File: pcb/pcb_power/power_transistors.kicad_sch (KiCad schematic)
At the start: 6 parts, among them Q1 BD139, Q2 BD139, Q3 BD249C, Q4 BD249C

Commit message: fin board
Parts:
- renumbered Q3 to Q40, Q1 to Q41, Q4 to Q42, Q2 to Q43, R1 to R40, R2 to R41
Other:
- note added: "30V 5A Linear Power Supply"

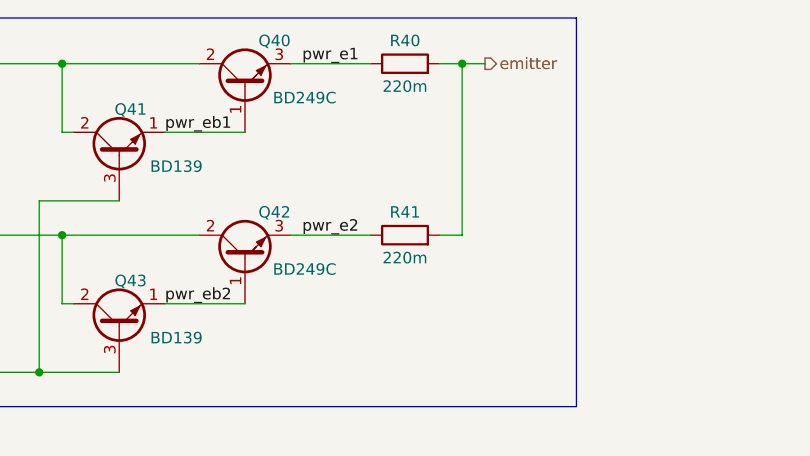
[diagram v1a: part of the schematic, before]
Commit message: adjust emiter resistors values, correct relay2 silkscreen, add gerbers
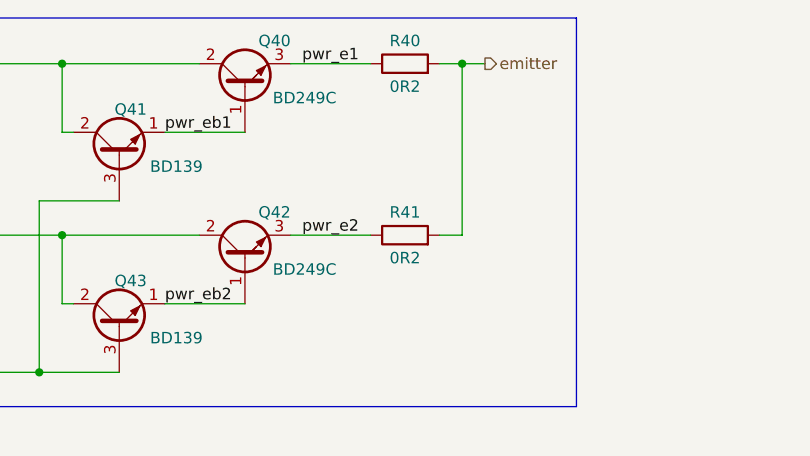
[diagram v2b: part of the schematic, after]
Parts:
- R40, R41: value 220m -> 0R2
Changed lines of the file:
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@@
 			)
 		)
-		(property "Value" "220m"
+		(property "Value" "0R2"
 			(at 130.81 71.12 90)
 			(effects
@@
 			)
 		)
-		(property "Value" "220m"
+		(property "Value" "0R2"
 			(at 130.81 52.07 90)
 			(effects
